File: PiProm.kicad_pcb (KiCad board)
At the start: 2 copper layers, 50.8 x 56.9 mm, 26 parts, among them J1 Raspberry_Pi_2_3, Q1 BSS84, U1 4040, U2 4040, U3 GTL2000, U4 27C160, U5 MC33063AD, U6 LM317L_SO8

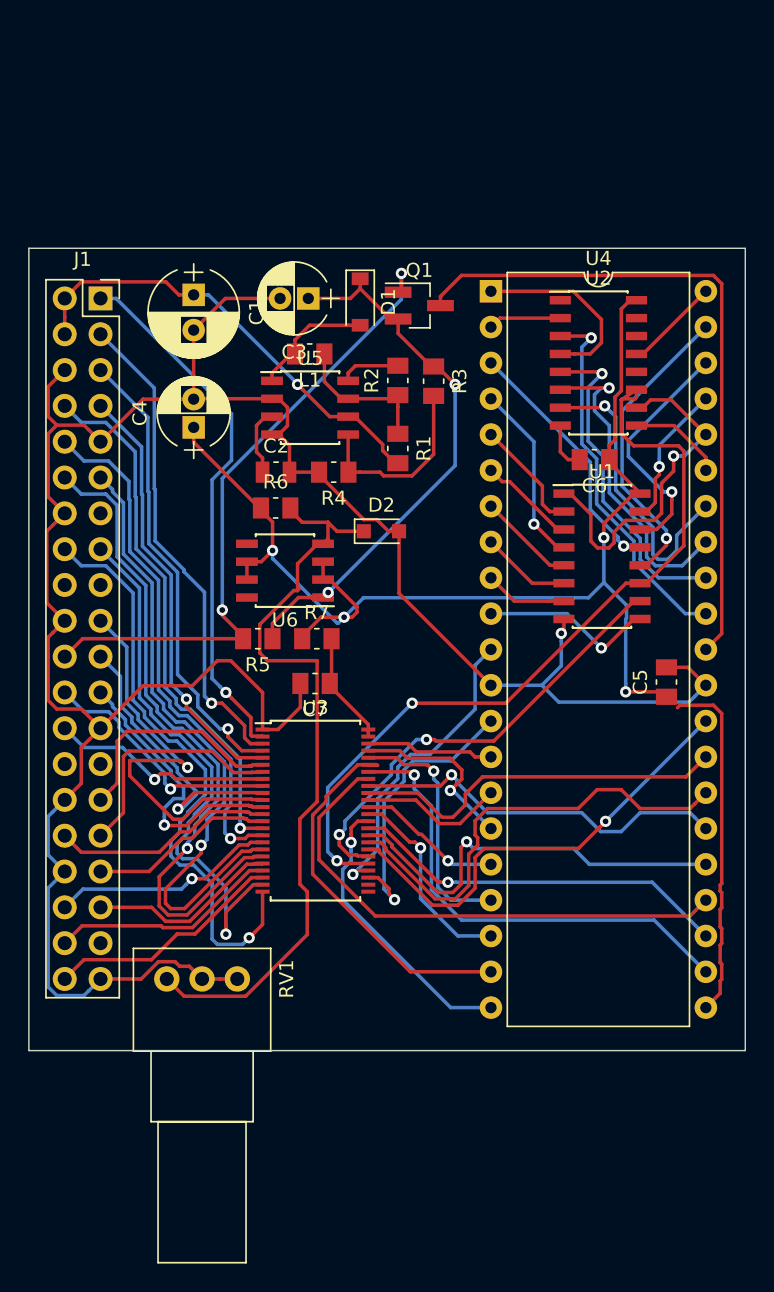
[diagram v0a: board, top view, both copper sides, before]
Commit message: Changed Step-Up Coil to Murata LQH32CN Re-arrange silkscreen labels
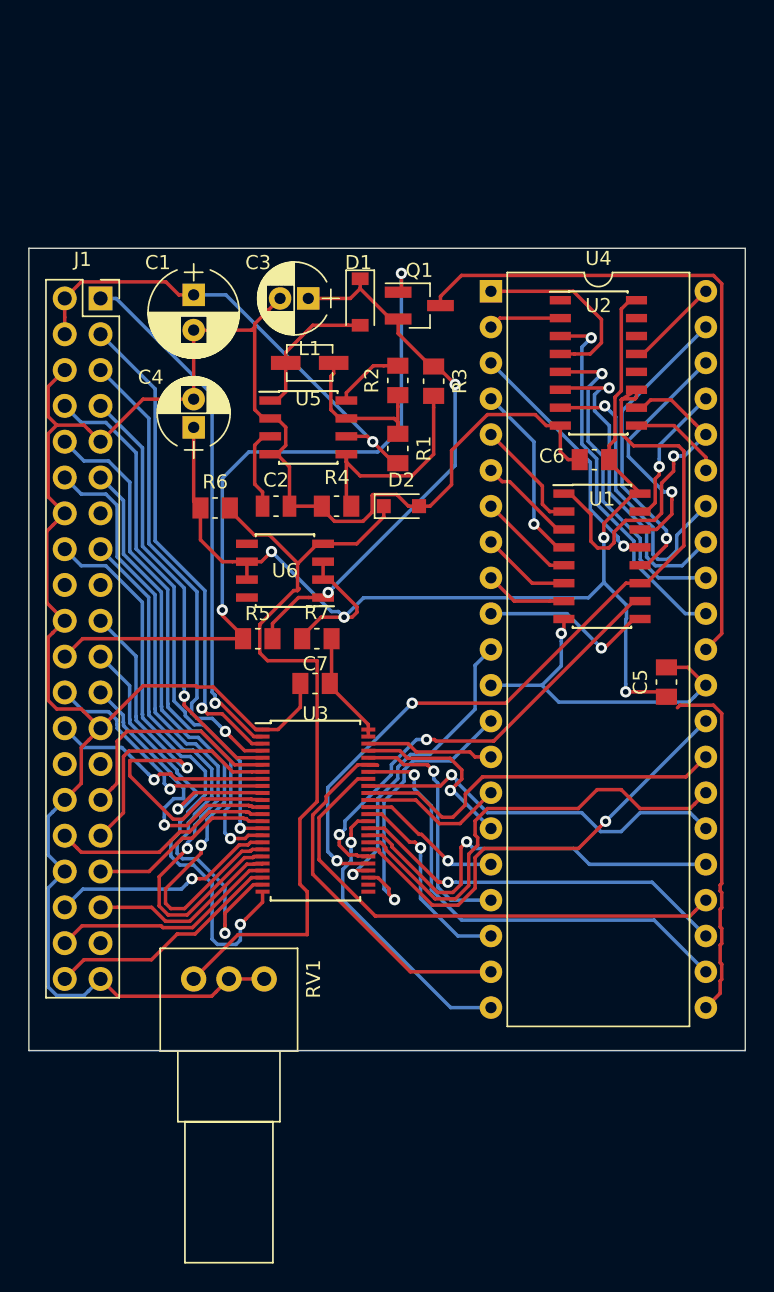
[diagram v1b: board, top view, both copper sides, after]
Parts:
- L1: footprint Inductor_SMD:L_0805_2012Metric_Pad1.15x1.50mm_HandSolder -> Murata:L_Murata_LQH32CN
- moved R6 4.29 mm to (25.9, 32.6)
- moved R4 2.42 mm to (34.5, 32.5)
- moved C2 2.41 mm to (30.2, 32.5)
- moved D2 2.27 mm to (39.1, 32.5)
- moved RV1 1.91 mm to (24.4, 66.0)
- moved U5 1.40 mm to (32.5, 26.9)
- moved L1 0.64 mm to (32.6, 22.4)
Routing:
- net GND: track 177.1 -> 183.5 mm
- net /Vpp_enable: track 46.4 -> 51.8 mm
- net Net-(L1-Pad1): track 10.5 -> 12.9 mm
- net Net-(R3-Pad2): track 13.6 -> 15.7 mm
- net /StepUpVoltage/V_in: track 32.2 -> 34.2 mm
- net Net-(D1-Pad2): track 8.79 -> 10.7 mm
- net Net-(C2-Pad1): track 4.85 -> 6.68 mm
- net Net-(D2-Pad1): track 55.2 -> 57.0 mm
- net Net-(R2-Pad2): track 4.29 -> 5.47 mm
- net Net-(J1-Pad1): track 38.0 -> 37.1 mm
- net /GPIO3: track 32.9 -> 33.4 mm

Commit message: Nice ground plane for switching regulator, thicker connections
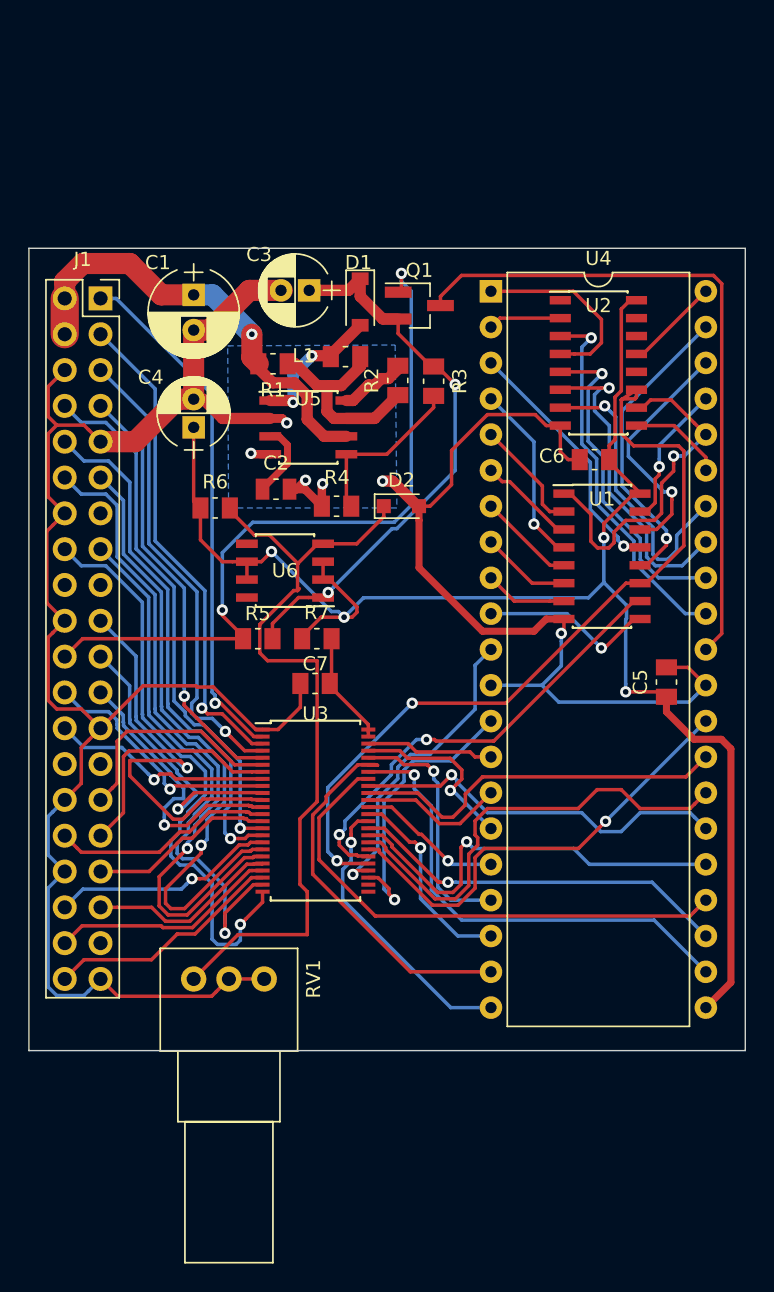
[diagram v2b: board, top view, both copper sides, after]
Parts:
- L1: footprint Murata:L_Murata_LQH32CN -> Inductor_SMD:L_0805_2012Metric_Pad1.15x1.50mm_HandSolder
- moved R1 10.7 mm to (30.0, 22.4), turned to 180 degrees
- moved L1 2.58 mm to (35.2, 21.9)
- moved C2 1.21 mm to (30.2, 31.3)
- moved C3 0.58 mm to (32.6, 17.2)
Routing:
- net GND: track 183.5 -> 193.1 mm, vias 1 -> 6
- net Net-(L1-Pad1): track 12.9 -> 17.7 mm
- net Net-(R3-Pad2): track 15.7 -> 12.2 mm
- net /StepUpVoltage/V_in: track 34.2 -> 31.5 mm
- net /Vpp_enable: track 51.8 -> 52.9 mm
- net Net-(C3-Pad1): track 39.6 -> 40.6 mm
- net VCC: track 112.4 -> 113.2 mm
- net Net-(D1-Pad2): track 10.7 -> 10.2 mm, vias 0 -> 2
- added copper zone on B.Cu, net GND

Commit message: Added optional bypass capacitor for LM317 Adj pin, to compensate for potentially long line to potentiometer
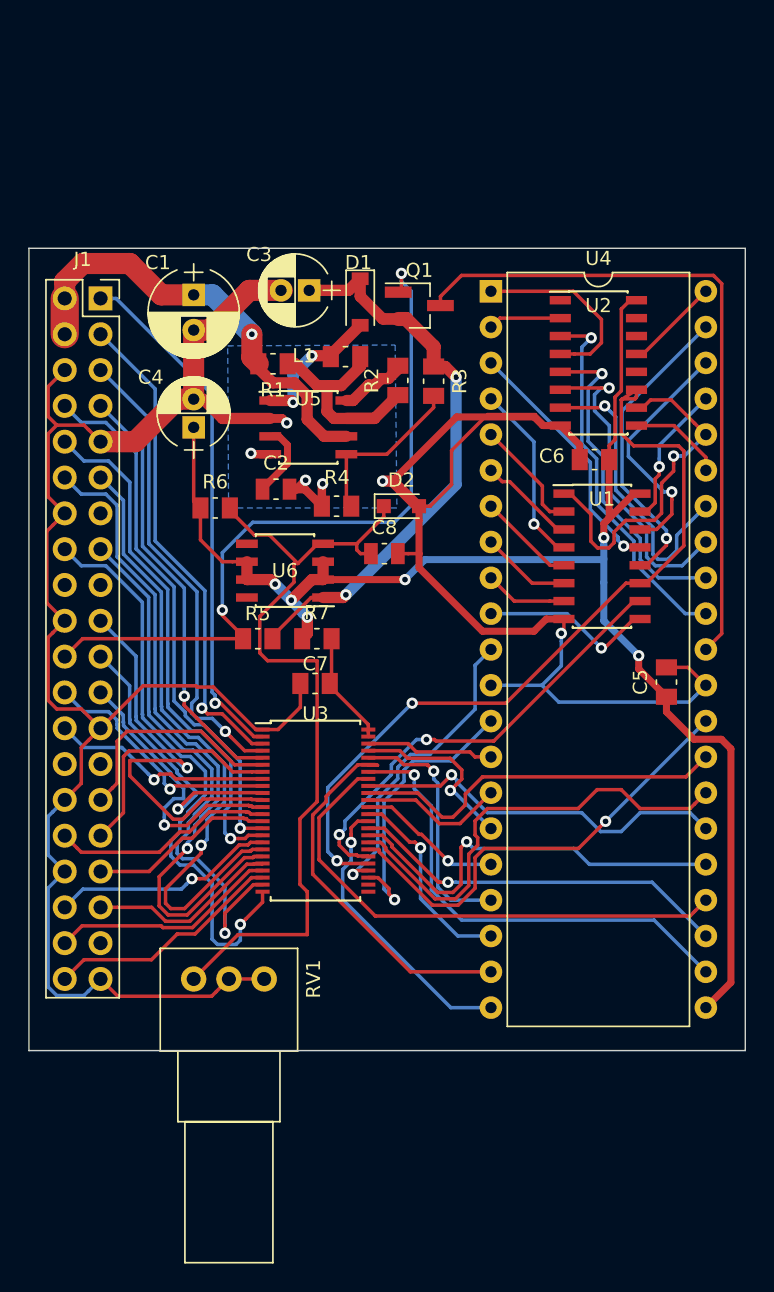
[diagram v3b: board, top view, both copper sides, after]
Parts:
- added C8: 10u, Capacitor_SMD:C_0805_2012Metric, F.Cu at (37.9, 35.9)
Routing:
- net GND: track 193.1 -> 208.1 mm
- net VCC: track 113.2 -> 110.4 mm, vias 4 -> 6
- net Net-(C8-Pad1): track 57.0 -> 58.4 mm
- net Net-(C3-Pad1): track 40.6 -> 41.7 mm

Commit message: New design: - Schematic in one file - Added boost driver for UV LED
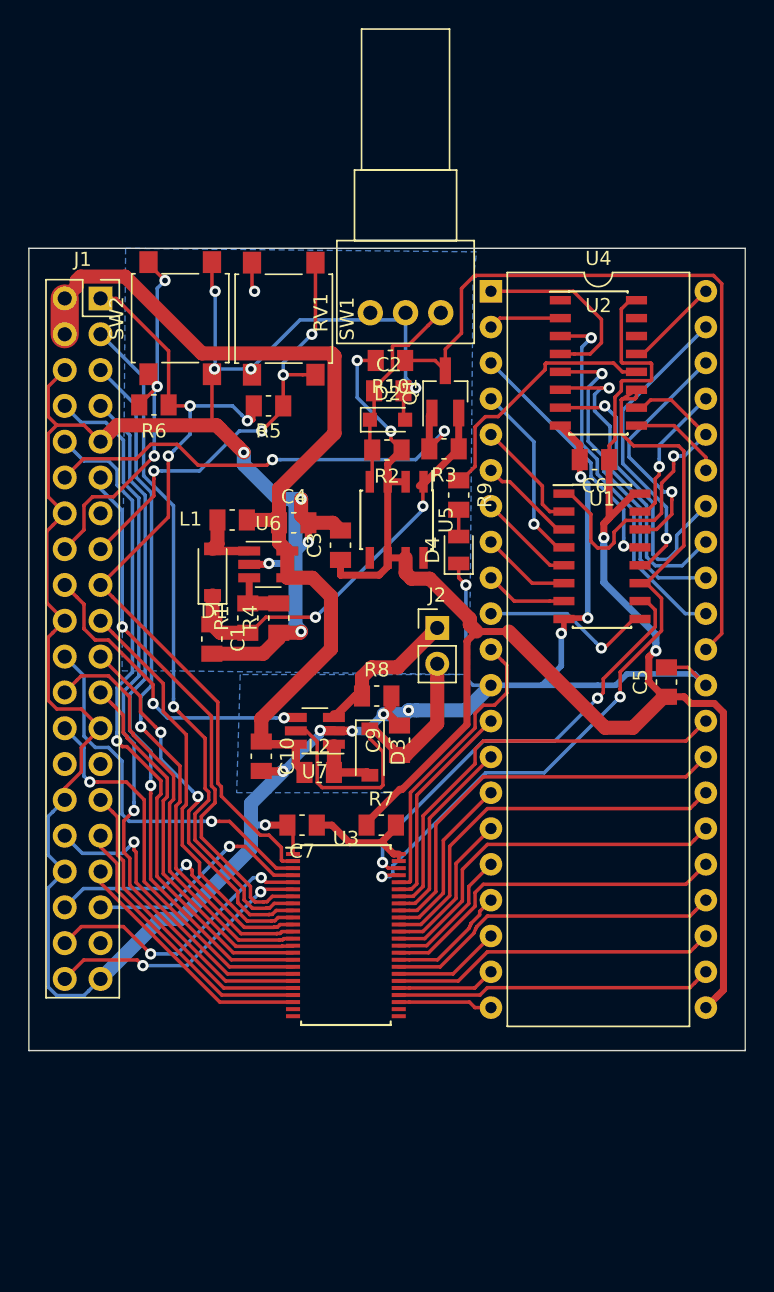
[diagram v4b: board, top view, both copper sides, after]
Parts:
- removed C8: 10u, Capacitor_SMD:C_0805_2012Metric
- added C10: 10u, Capacitor_SMD:C_0805_2012Metric_Pad1.15x1.50mm_HandSolder, F.Cu at (29.2, 50.2)
- added C9: 10u, Capacitor_SMD:C_0805_2012Metric_Pad1.15x1.50mm_HandSolder, F.Cu at (39.0, 49.1)
- added D3: SB120, Diode_SMD:D_SOD-123, F.Cu at (36.9, 49.9)
- added D4: LED, Diode_SMD:D_0805_2012Metric_Pad0.97x1.50mm_HandSolder, F.Cu at (43.2, 35.6)
- added J2: Conn_01x02_Male, Connector_PinHeader_2.54mm:PinHeader_1x02_P2.54mm_Vertical, F.Cu at (41.7, 41.1)
- added L2: 2u2, Inductor_SMD:L_0805_2012Metric_Pad1.15x1.50mm_HandSolder, F.Cu at (33.3, 51.4)
- added R10: 10k, Resistor_SMD:R_0805_2012Metric_Pad1.15x1.50mm_HandSolder, F.Cu at (38.3, 22.2)
- added R8: 5.28, Resistor_SMD:R_0805_2012Metric_Pad1.15x1.50mm_HandSolder, F.Cu at (37.4, 46.0)
- added R9: R, Resistor_SMD:R_0805_2012Metric_Pad1.15x1.50mm_HandSolder, F.Cu at (43.2, 31.7)
- added SW1: SW_Push, Button_Switch_SMD:SW_SPST_B3S-1000, F.Cu at (30.8, 19.2)
- added SW2: SW_Push, Button_Switch_SMD:SW_SPST_B3S-1000, F.Cu at (23.4, 19.2)
- added U7: PT4101, Package_TO_SOT_SMD:SOT-23-6_Handsoldering, F.Cu at (33.0, 48.4)
- C1: value 470u -> 1u; footprint Capacitor_THT:CP_Radial_D6.3mm_P2.50mm -> Capacitor_SMD:C_0805_2012Metric_Pad1.15x1.50mm_HandSolder
- C2: value 470p -> 10u; footprint Capacitor_SMD:C_0805_2012Metric -> Capacitor_SMD:C_0805_2012Metric_Pad1.15x1.50mm_HandSolder
- C3: value 100u -> 10u; footprint Capacitor_THT:CP_Radial_D5.0mm_P2.00mm -> Capacitor_SMD:C_0805_2012Metric_Pad1.15x1.50mm_HandSolder
- C4: value 10u -> 1u; footprint Capacitor_THT:CP_Radial_D5.0mm_P2.00mm -> Capacitor_SMD:C_0805_2012Metric_Pad1.15x1.50mm_HandSolder
- L1: value 100u -> 10u
- R1: value 0.22 -> 15k
- R2: value 220 -> 1k5
- R5: value 15k -> R
- R6: value 1k5 -> R
- U5: value MC33063AD -> LM317L_SO8
- U6: value LM317L_SO8 -> AP3012; footprint Package_SOIC:SOIC-8_3.9x4.9mm_P1.27mm -> Package_TO_SOT_SMD:SOT-23-5_HandSoldering
- moved RV1 50.4 mm to (41.9, 18.8), turned to 90 degrees
- moved C1 24.4 mm to (25.7, 41.9)
- moved D1 21.8 mm to (25.7, 37.2), turned to 90 degrees
- moved C3 18.2 mm to (34.8, 35.3), turned to 90 degrees
- moved R1 18.1 mm to (28.2, 40.4), turned to 90 degrees
- moved R5 16.5 mm to (29.7, 25.4), turned to 0 degrees
- moved L1 14.1 mm to (27.1, 33.5)
- moved R7 14.0 mm to (37.7, 55.1)
- moved C2 10.6 mm to (38.2, 24.3)
- moved C7 10.1 mm to (32.1, 55.1)
- moved C4 9.80 mm to (31.5, 33.7), turned to 0 degrees
- moved U3 9.09 mm to (35.2, 62.9)
- moved U5 9.07 mm to (38.8, 33.5), turned to 270 degrees
- moved R4 8.93 mm to (30.4, 40.4), turned to 270 degrees
- moved R6 8.50 mm to (21.6, 25.3), turned to 180 degrees
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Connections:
- net /GPIO26 renamed Net-(J1-Pad13)
- net /Vpp renamed VPP
- C1 pad 1: /StepUpVoltage/V_in -> Net-(C1-Pad1)
- C3 pad 1: Net-(C3-Pad1) -> VCC
- C4 pad 1: VCC -> +5V
- D1 pad 1: Net-(C3-Pad1) -> Net-(C1-Pad1)
- D2 pad 1: Net-(C8-Pad1) -> Net-(C2-Pad1)
- J1 pad 1: Net-(J1-Pad1) -> +3V3
- J1 pad 12: /GPIO18 -> /Vpp_enable
- J1 pad 15: /GPIO22 -> /BUTTON1
- J1 pad 16: /GPIO23 -> /BUTTON2
- J1 pad 17: Net-(J1-Pad17) -> +3V3
- J1 pad 18: /GPIO24 -> /LED_enable
- J1 pad 2: /StepUpVoltage/V_in -> +5V
- J1 pad 22: /Vpp_enable -> /GPIO25
- J1 pad 37: /GPIO25 -> Net-(J1-Pad37)
- J1 pad 4: /StepUpVoltage/V_in -> +5V
- L1 pad 1: Net-(L1-Pad1) -> +5V
- Q1 pad 2: Net-(C3-Pad1) -> Net-(C1-Pad1)
- R1 pad 1: Net-(L1-Pad1) -> Net-(C1-Pad1)
- R1 pad 2: /StepUpVoltage/V_in -> Net-(R1-Pad2)
- R2 pad 1: Net-(L1-Pad1) -> VCC
- R2 pad 2: Net-(R2-Pad2) -> Net-(C2-Pad1)
- R3 pad 1: Net-(C3-Pad1) -> Net-(C1-Pad1)
- R3 pad 2: Net-(R3-Pad2) -> /Vpp_enable
- R4 pad 1: Net-(R3-Pad2) -> Net-(R1-Pad2)
- R5 pad 1: Net-(C3-Pad1) -> +3V3
- R5 pad 2: /Vpp_enable -> /BUTTON1
- R6 pad 1: VCC -> +3V3
- R6 pad 2: Net-(C8-Pad1) -> /BUTTON2
- RV1 pad 1: Net-(C8-Pad1) -> Net-(C2-Pad1)
- U3 pad 10: /GPIO9 -> /GPIO10
- U3 pad 11: /GPIO10 -> /GPIO16
- U3 pad 12: /GPIO11 -> /GPIO3
- U3 pad 13: /GPIO12 -> /GPIO8
- U3 pad 14: /GPIO13 -> /GPIO11
- U3 pad 15: /GPIO14 -> /GPIO15
- U3 pad 16: /GPIO15 -> /GPIO4
- U3 pad 17: /GPIO16 -> /GPIO7
- U3 pad 18: /GPIO17 -> /GPIO12
- U3 pad 19: /GPIO18 -> /GPIO14
- U3 pad 2: Net-(J1-Pad1) -> +3V3
- U3 pad 20: /GPIO19 -> /GPIO5
- U3 pad 21: /GPIO20 -> /GPIO6
- U3 pad 22: /GPIO21 -> /GPIO13
- U3 pad 23: /GPIO22 -> Net-(U3-Pad23)
- U3 pad 24: /GPIO23 -> Net-(U3-Pad24)
- U3 pad 27: /OE -> /D11
- U3 pad 28: /CE -> /D4
- U3 pad 29: /ADDR_RST -> /D3
- U3 pad 3: /GPIO2 -> /GPIO25
- U3 pad 30: /ADDR_CLK -> /D12
- U3 pad 31: /D15 -> /D10
- U3 pad 32: /D14 -> /D5
- U3 pad 33: /D13 -> /D2
- U3 pad 34: /D12 -> /D13
- U3 pad 35: /D11 -> /D9
- U3 pad 36: /D10 -> /D6
- U3 pad 37: /D9 -> /D1
- U3 pad 38: /D8 -> /D14
- U3 pad 39: /D7 -> /D8
- U3 pad 4: /GPIO3 -> /GPIO19
- U3 pad 40: /D6 -> /D7
- U3 pad 41: /D5 -> /D0
- U3 pad 42: /D4 -> /D15
- U3 pad 43: /D3 -> /OE
- U3 pad 44: /D2 -> /CE
- U3 pad 45: /D1 -> /ADDR_RST
- U3 pad 46: /D0 -> /ADDR_CLK
- U3 pad 5: /GPIO4 -> /GPIO20
- U3 pad 6: /GPIO5 -> /GPIO21
- U3 pad 7: /GPIO6 -> /GPIO17
- U3 pad 8: /GPIO7 -> /GPIO2
- U3 pad 9: /GPIO8 -> /GPIO9
- U5 pad 1: Net-(D1-Pad2) -> Net-(C1-Pad1)
- U5 pad 2: GND -> VCC
- U5 pad 3: Net-(C2-Pad1) -> VCC
- U5 pad 4: GND -> Net-(C2-Pad1)
- U5 pad 5: Net-(R3-Pad2) -> Net-(U5-Pad5)
- U5 pad 6: /StepUpVoltage/V_in -> VCC
- U5 pad 7: Net-(L1-Pad1) -> VCC
- U5 pad 8: Net-(R2-Pad2) -> Net-(U5-Pad8)
- U6 pad 1: Net-(C3-Pad1) -> Net-(D1-Pad2)
- U6 pad 2: VCC -> GND
- U6 pad 3: VCC -> Net-(R1-Pad2)
- U6 pad 4: Net-(C8-Pad1) -> +5V
- U6 pad 5: Net-(U6-Pad5) -> +5V
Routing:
- net +5V: track 0.00 -> 65.6 mm
- net +3V3: track 0.00 -> 59.1 mm, vias 0 -> 3
- net Net-(C8-Pad1): track 58.4 -> 0.00 mm
- net /GPIO18: track 47.3 -> 0.00 mm, vias 1 -> 0
- net /GPIO23: track 42.4 -> 0.00 mm, vias 1 -> 0
- net Net-(C3-Pad1): track 41.7 -> 0.00 mm, vias 2 -> 0
- net /GPIO22: track 38.8 -> 0.00 mm, vias 1 -> 0
- net Net-(J1-Pad1): track 37.1 -> 0.00 mm, vias 1 -> 0
- net GND: track 208.1 -> 242.7 mm, vias 6 -> 20
- net /BUTTON1: track 0.00 -> 31.7 mm, vias 0 -> 4
- net /StepUpVoltage/V_in: track 31.5 -> 0.00 mm, vias 1 -> 0
- net Net-(C1-Pad1): track 0.00 -> 29.4 mm, vias 0 -> 2
- net /BUTTON2: track 0.00 -> 27.6 mm, vias 0 -> 3
- net /GPIO25: track 0.00 -> 27.1 mm, vias 0 -> 1
- net VCC: track 110.4 -> 137.0 mm, vias 6 -> 4
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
